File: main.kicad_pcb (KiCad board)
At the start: 2 copper layers, 32 x 32 mm, 46 parts, among them J1 USB_OTG, J2 Conn_01x02, J4 Conn_01x02, J5 Conn_02x03_Odd_Even, J6 Conn_01x02, Q1 Q_PMOS_GSD, Q2 NTLJF3117P, SW1 SW_Push, SW2 SW_SPDT, U1 LTC2955-1(DFN), U2 LTC3458, U3 ATTINY13-20SSU, U4 MCP73831

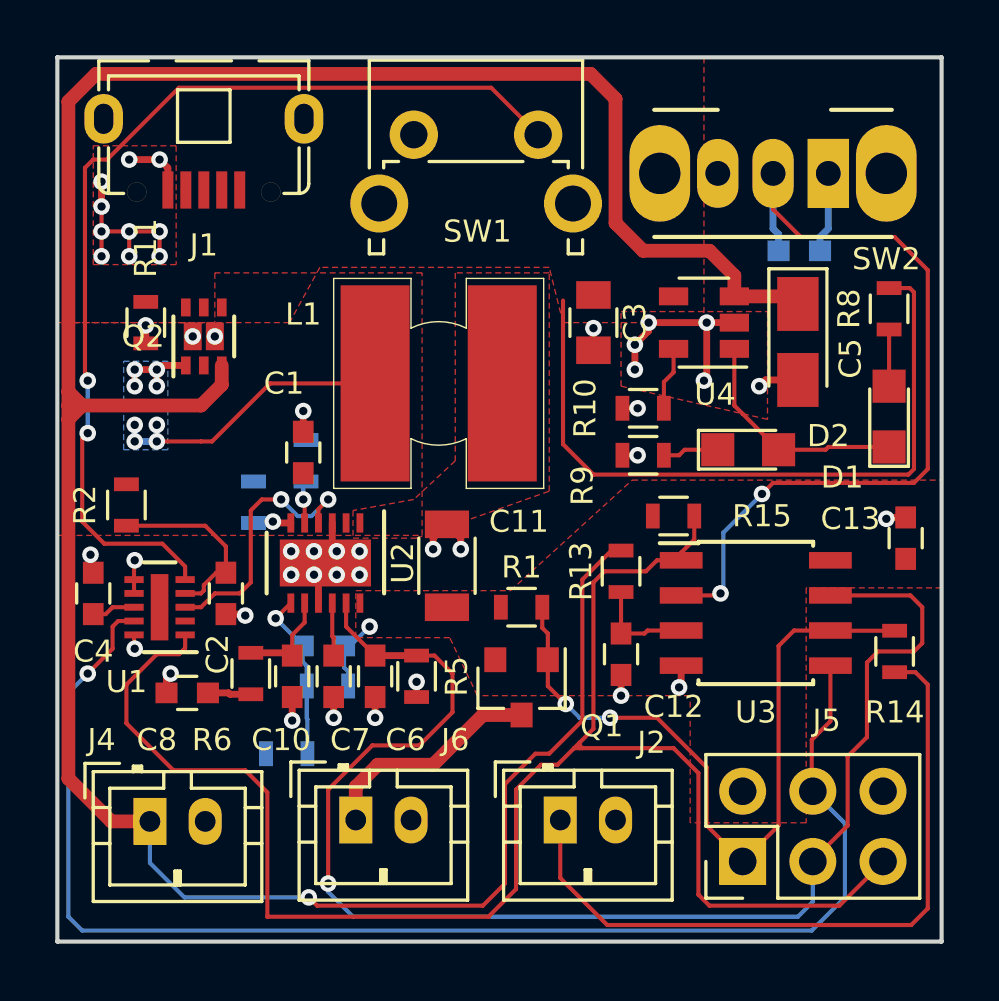
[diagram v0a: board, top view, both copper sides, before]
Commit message: Fixed NTLJF3117P MOSFET pin layout
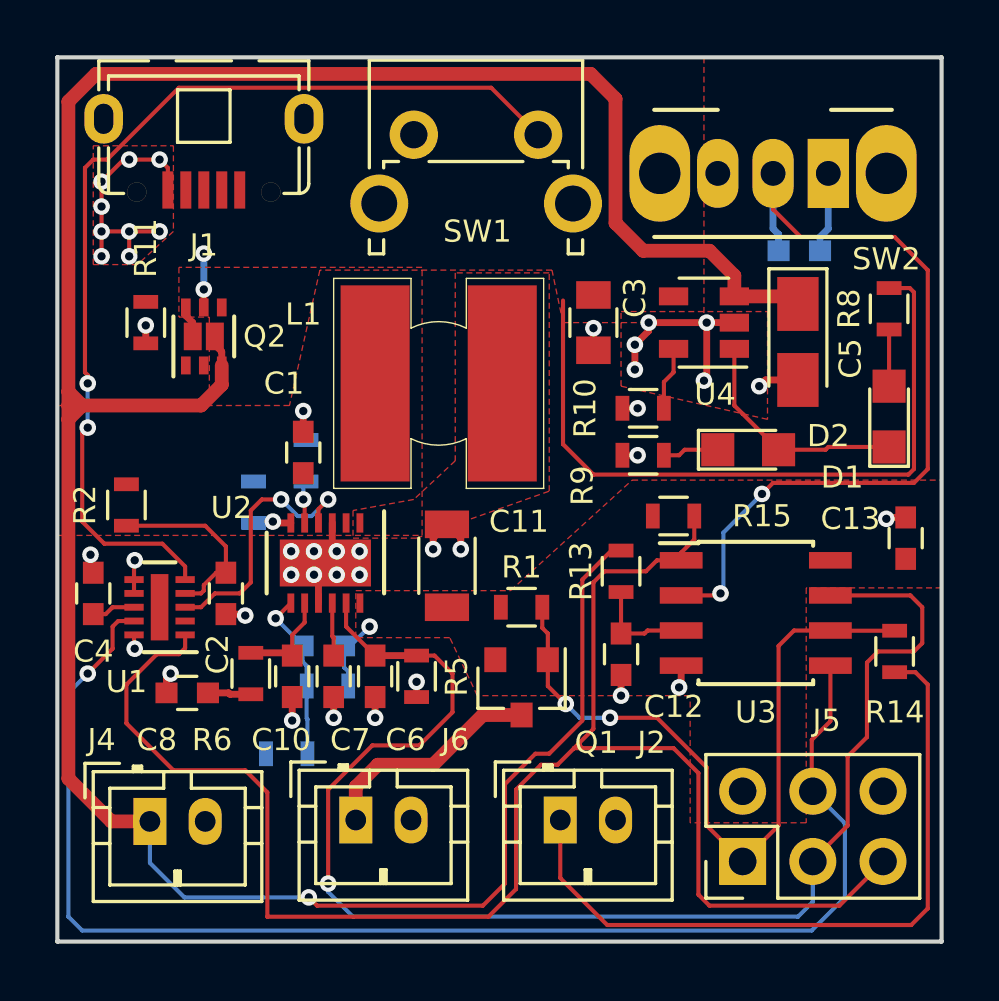
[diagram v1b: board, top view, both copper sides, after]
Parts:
- D1: value LED -> Red LED
- D2: value LED -> Green LED
- Q1: value Q_PMOS_GSD -> DMP1045U
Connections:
- Q2 pad 1: /Power Supply/DC/DC boost converter/Vsup -> /Power Supply/VUSB
- Q2 pad 6: /Power Supply/VUSB -> /Power Supply/DC/DC boost converter/Vsup
- Q2 pad 7: GND -> /Power Supply/DC/DC boost converter/Vsup
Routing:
- net /Power Supply/DC/DC boost converter/Vsup: track 13.9 -> 1.15 mm, vias 8 -> 0
- net GND: track 30.6 -> 37.7 mm, vias 37 -> 42
- net (no net): track 6.60 -> 0.00 mm, vias 8 -> 0
- net /Power Supply/VUSB: track 25.8 -> 27.8 mm, vias 0 -> 2
- net /BAT+: track 99.0 -> 100.2 mm
- removed copper zone on B.Cu, net /Power Supply/DC/DC boost converter/Vsup
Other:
- board text added: "Programmable Heater v1.1 Design: Patrick Baus Date: 2017-10 https://github.com/PatrickBaus"
- board text removed: "Programmable Heater Design: Patrick Baus Date: 2017-10 https://github.com/PatrickBaus"

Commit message: Moved MCU pins around to make sure that they do not interfere with the programmer Moved ISP Header closer to the edge of the board to allow easier access with the programmer Added pulldown resistor to the DCD/DC converters enable pin to make sure it stays off in case of failure Added more PDFs of components
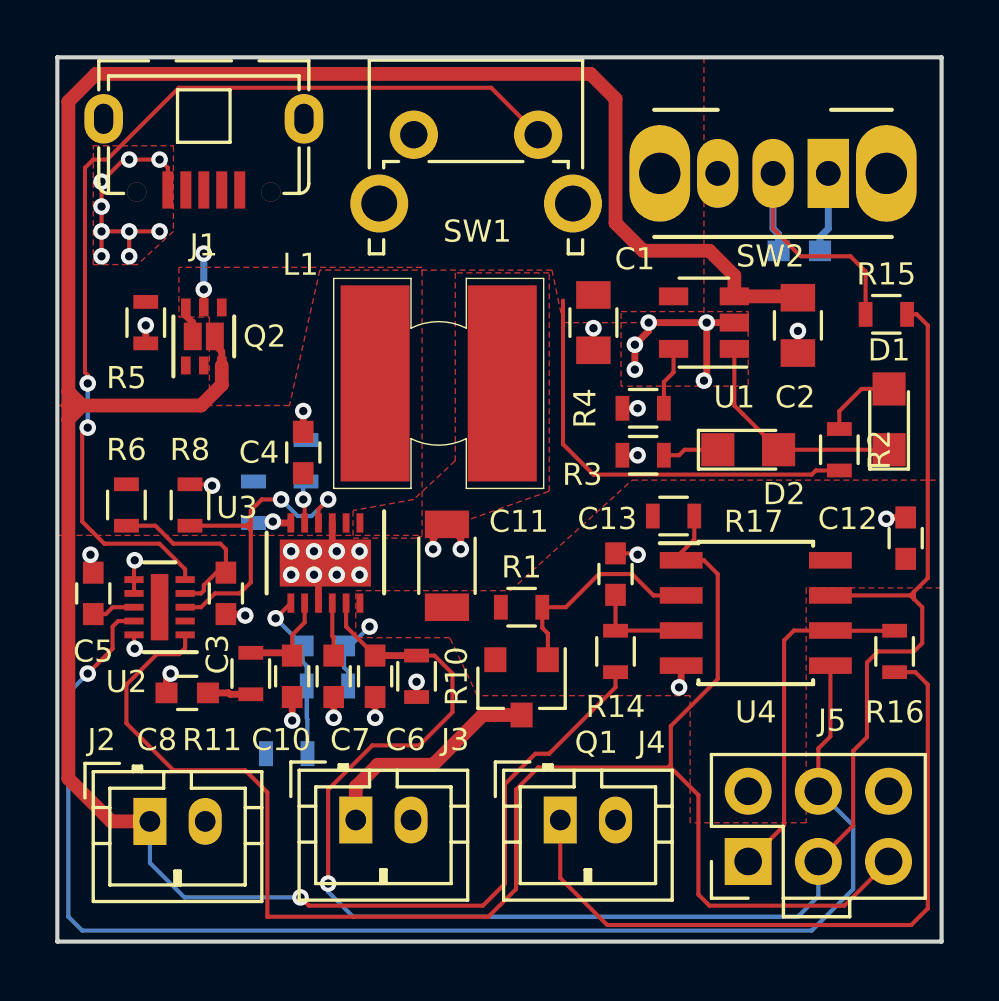
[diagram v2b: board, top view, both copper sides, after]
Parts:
- removed the C5 at (116.8, 80.3)
- added C2: 10u, Capacitors_SMD:C_0805, F.Cu at (116.8, 79.7)
- added R15: 4.7k, Resistors_SMD:R_0603, F.Cu at (120.0, 79.3)
- added R8: 100k, Resistors_SMD:R_0603, F.Cu at (94.8, 86.2)
- J5: value Conn_02x03_Odd_Even -> AVR-ISP-6
- moved R2 5.41 mm to (118.3, 84.2), turned to 270 degrees
- moved R14 2.91 mm to (110.2, 91.5), turned to 270 degrees
- moved C13 2.91 mm to (110.2, 88.7), turned to 90 degrees
- moved J5 0.20 mm to (115.0, 99.1)
- moved D1 0.10 mm to (120.1, 83.1)
- renumbered C3 to C1, C13 to C12, C12 to C13, C2 to C3, C1 to C4, C4 to C5, J4 to J2, J6 to J3, J2 to J4, R5 to R10, R6 to R11, R7 to R12, R12 to R13, R13 to R14, R14 to R16, R15 to R17, R8 to R2, R9 to R3, R10 to R4, R11 to R5, R2 to R6, R3 to R7, R4 to R9, U4 to U1, U1 to U2, U2 to U3, U3 to U4
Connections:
- C6 pad 1: /Microcontroller/~enable_burst -> Net-(C6-Pad1)
- J5 pad 1: /Microcontroller/~enable_heater -> /Microcontroller/MISO
- J5 pad 3: /Microcontroller/~enable_burst -> /Microcontroller/SCK
- J5 pad 5: /Power Supply/Power_down_warning -> /Microcontroller/RST
- R10 pad 1: /Microcontroller/~enable_burst -> Net-(C6-Pad1)
- R16 pad 1: /Microcontroller/~enable_heater -> /Microcontroller/MISO
- R17 pad 2: /Power Supply/Power_down_warning -> /Microcontroller/RST
- U2 pad 1: /Power Supply/Power_down_warning -> Net-(U2-Pad1)
- U3 pad 11: /Microcontroller/~enable_burst -> Net-(C6-Pad1)
- U4 pad 1: /Power Supply/Power_down_warning -> /Microcontroller/RST
- U4 pad 2: Net-(C14-Pad1) -> /Microcontroller/~enable_heater
- U4 pad 6: /Microcontroller/~enable_heater -> /Microcontroller/MISO
- U4 pad 7: /Microcontroller/~enable_burst -> /Microcontroller/SCK
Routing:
- net /Power Supply/Power_down_warning: track 59.6 -> 0.00 mm
- net /Microcontroller/RST: track 0.00 -> 56.5 mm
- net /Microcontroller/~enable_burst: track 50.9 -> 0.00 mm, vias 1 -> 0
- net /Microcontroller/SCK: track 0.00 -> 44.7 mm
- net Net-(C14-Pad1): track 29.9 -> 10.4 mm, vias 2 -> 0
- net /Microcontroller/~enable_heater: track 26.6 -> 7.83 mm, vias 2 -> 0
- net Net-(C6-Pad1): track 0.00 -> 17.4 mm, vias 0 -> 1
- net /Microcontroller/MISO: track 0.00 -> 12.7 mm
- net /Power Supply/VUSB: track 27.8 -> 17.7 mm
- net /BAT+: track 100.2 -> 95.5 mm
- net Net-(R8-Pad1): track 9.81 -> 12.5 mm
- net Net-(U2-Pad1): track 0.00 -> 1.59 mm
- net Net-(D1-Pad2): track 2.05 -> 2.78 mm
- net GND: track 37.7 -> 37.9 mm, vias 42 -> 43
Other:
- board text added: "Programmable Heater v1.1 Design: Patrick Baus Date: 2018-01 https://github.com/PatrickBaus"
- board text removed: "Programmable Heater v1.1 Design: Patrick Baus Date: 2017-10 https://github.com/PatrickBaus"

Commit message: Preparing for v1.2 Updated to KiCAD 5 nightly Added resistors to isolate the programming pins Added transistor to drive the LED Replaced LTC3458 boost converter with an LTC3536 buck-boost converter to step down the USB power supply Added debugging jumper to test the voltage regulator
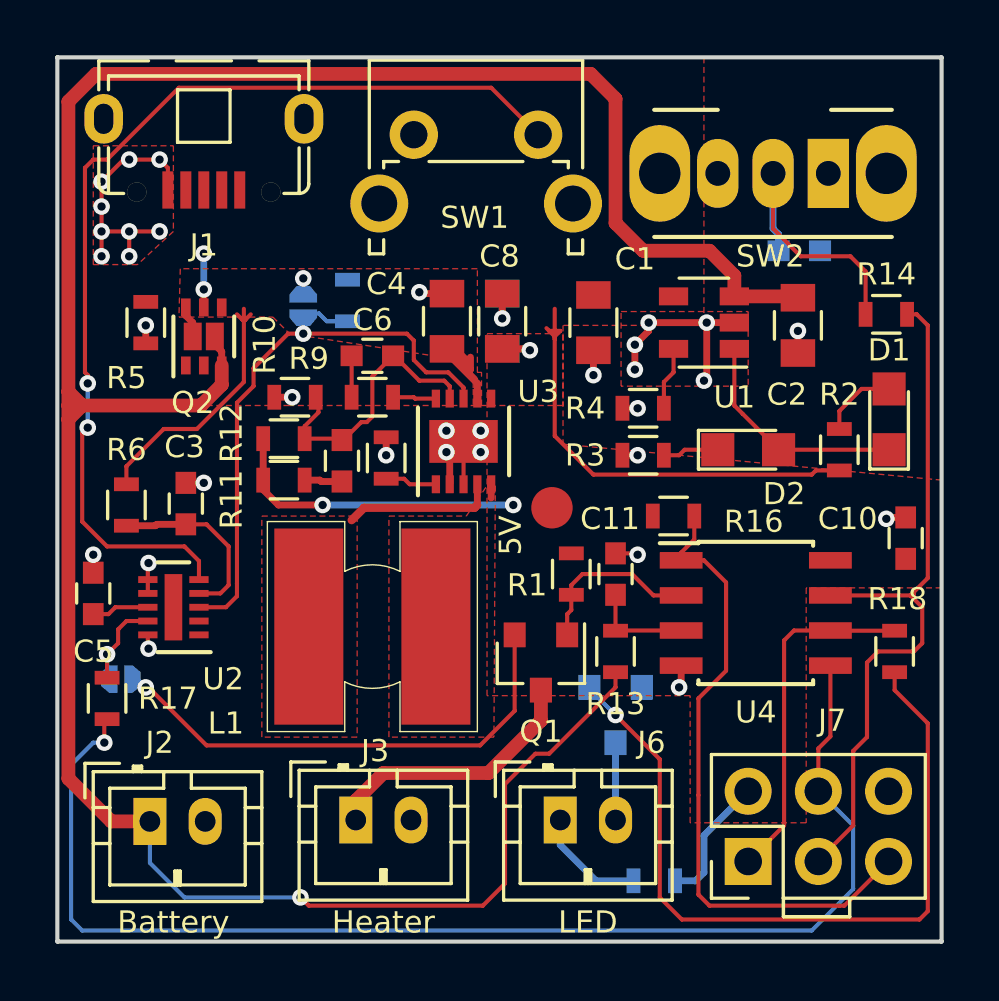
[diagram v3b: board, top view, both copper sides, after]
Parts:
- removed the C10 at (98.5, 92.4)
- removed the C11 at (104.1, 88.4)
- removed the R13 at (98.3, 95.2)
- removed REF***: OSHW-Logo_7.5x8mm_SilkScreen, Symbols:OSHW-Logo_7.5x8mm_SilkScreen
- added J4: GS2, Custom_footprints:jumper_solder_small, B.Cu at (98.9, 79.0)
- added J5: GS2, Custom_footprints:jumper_solder_small, B.Cu at (92.3, 92.5)
- added J8: Conn_01x01, Measurement_Points:Measurement_Point_Round-SMD-Pad_Small, F.Cu at (107.9, 86.3)
- added Q3: MMBT3904, TO_SOT_Packages_SMD:SOT-23, B.Cu at (110.2, 93.8)
- added R17: 4.7k, Resistors_SMD:R_0603, F.Cu at (91.8, 93.2)
- added R18: 4.7k, Resistors_SMD:R_0603, F.Cu at (120.3, 91.5)
- C4: value 2.2u -> 47u; footprint Capacitors_SMD:C_0603 -> Capacitors_SMD:C_0805
- C6: value 10n -> 200p
- C7: value 10n -> 18p
- C8: value 560p -> 47u; footprint Capacitors_SMD:C_0603 -> Capacitors_SMD:C_0805
- C9: value 10p -> 47u; footprint Capacitors_SMD:C_0603 -> Capacitors_SMD:C_0805
- R10: value 133k -> 150k
- R11: value 33k -> 22.6k
- R12: value 1M -> 1.1M; moved to F.Cu
- R15: renamed from R16; moved to B.Cu
- R7: renamed from R8; moved to B.Cu
- R8: renamed from R7; value 450k -> 332k; moved to F.Cu
- R9: value 124k -> 33k; moved to F.Cu
- SW1: footprint SW_Tactile_SPST_Angled_PTS645Vx31-2LFS -> Buttons_Switches_THT:SW_Tactile_SPST_Angled_PTS645Vx31-2LFS
- U3: value LTC3458 -> LTC3536; footprint Housings_DFN_QFN:DFN-12-1EP_3x4mm_Pitch0.5mm -> Housings_DFN_QFN:DFN-10-1EP_3x3mm_Pitch0.5mm
- U4: value ATTINY13-20SSU -> ATTINY13
- moved C8 17.6 mm to (106.1, 79.5), turned to 90 degrees
- moved C9 13.4 mm to (106.1, 79.5), turned to 90 degrees
- moved R15 12.0 mm to (111.6, 99.8), turned to 180 degrees
- moved C6 11.6 mm to (101.4, 80.8), turned to 0 degrees
- moved R10 11.0 mm to (98.6, 82.3), turned to 180 degrees
- moved R7 9.34 mm to (100.5, 78.8)
- moved L1 9.12 mm to (101.4, 90.6)
- moved R12 9.09 mm to (98.2, 83.8), turned to 0 degrees
- moved C7 7.81 mm to (100.3, 84.6), turned to 90 degrees
- moved R11 7.10 mm to (98.2, 85.3), turned to 0 degrees
- moved C4 7.04 mm to (104.1, 79.5)
- moved U3 6.66 mm to (104.7, 83.9), turned to 90 degrees
- moved R8 5.06 mm to (101.9, 84.5)
- moved C3 3.56 mm to (94.7, 86.2), turned to 90 degrees
- moved R9 3.32 mm to (101.4, 82.3), turned to 0 degrees
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- renumbered C12 to C10, C13 to C11, C14 to C12, J4 to J6, J5 to J7, R14 to R13, R15 to R14, R17 to R16
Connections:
- C6 pad 2: GND -> Net-(C6-Pad2)
- C7 pad 2: GND -> Net-(C6-Pad2)
- C8 pad 1: Net-(C8-Pad1) -> /Power Supply/V+5
- C9 pad 2: Net-(C9-Pad2) -> GND
- J6 pad 2: GND -> Net-(J6-Pad2)
- J7 pad 4: /Power Supply/Kill_power -> /Microcontroller/MOSI
- L1 pad 1: /Power Supply/DC/DC boost converter/Vsup -> Net-(L1-Pad1)
- R10 pad 1: Net-(C6-Pad1) -> Net-(C6-Pad2)
- R11 pad 1: Net-(C10-Pad1) -> /Power Supply/V+5
- R11 pad 2: Net-(C8-Pad1) -> Net-(C7-Pad1)
- R12 pad 2: Net-(C9-Pad2) -> Net-(C6-Pad2)
- R15 pad 1: /Microcontroller/MISO -> /Power Supply/V+5
- R7 pad 1: Net-(R8-Pad1) -> Net-(J4-Pad2)
- R8 pad 1: Net-(R7-Pad1) -> Net-(R8-Pad1)
- R9 pad 1: Net-(R9-Pad1) -> Net-(C6-Pad1)
- R9 pad 2: GND -> Net-(R9-Pad2)
- U2 pad 3: Net-(R8-Pad1) -> Net-(J4-Pad2)
- U2 pad 9: /Power Supply/Kill_power -> /Power Supply/~Kill_power
- U3 pad 1: Net-(L1-Pad2) -> Net-(R8-Pad1)
- U3 pad 10: Net-(C7-Pad1) -> Net-(R9-Pad2)
- U3 pad 11: Net-(C6-Pad1) -> GND
- U3 pad 2: /Power Supply/DC/DC boost converter/Vsup -> GND
- U3 pad 4: Net-(R8-Pad1) -> Net-(L1-Pad1)
- U3 pad 5: Net-(R9-Pad1) -> Net-(L1-Pad2)
- U3 pad 6: Net-(R7-Pad1) -> /Power Supply/V+5
- U3 pad 7: Net-(C9-Pad2) -> /Power Supply/DC/DC boost converter/Vsup
- U3 pad 8: Net-(C10-Pad1) -> Net-(J4-Pad2)
- U3 pad 9: GND -> Net-(C6-Pad2)
- U4 pad 5: /Power Supply/Kill_power -> /Microcontroller/MOSI
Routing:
- net /Power Supply/Kill_power: track 50.1 -> 0.00 mm, vias 1 -> 0
- net /Microcontroller/MOSI: track 0.00 -> 45.9 mm, vias 0 -> 1
- net /Power Supply/V+5: track 2.73 -> 36.1 mm, vias 1 -> 4
- net /Microcontroller/RST: track 56.5 -> 23.2 mm
- net Net-(Q3-Pad1): track 0.00 -> 28.0 mm, vias 0 -> 1
- net Net-(J4-Pad2): track 0.00 -> 22.2 mm, vias 0 -> 1
- net Net-(J6-Pad1): track 25.8 -> 4.09 mm
- net /Microcontroller/SCK: track 44.7 -> 26.2 mm
- net /Power Supply/DC/DC boost converter/Vsup: track 1.15 -> 17.6 mm, vias 0 -> 1
- net Net-(C6-Pad1): track 17.4 -> 1.50 mm, vias 1 -> 0
- net Net-(R8-Pad1): track 12.5 -> 1.88 mm, vias 2 -> 0
- net Net-(C6-Pad2): track 0.00 -> 10.00 mm
- net Net-(C9-Pad2): track 6.15 -> 0.00 mm, vias 1 -> 0
- net Net-(L1-Pad1): track 0.00 -> 5.53 mm
- net GND: track 37.9 -> 32.7 mm, vias 43 -> 34
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- added copper zone on F.Cu, net Net-(L1-Pad1)
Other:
- board text added: "5V"
- board text added: "A"
- board text added: "C"
- board text added: "GND"
- board text added: "MISO"
- board text added: "MOSI"
- board text added: "Programmable Heater v1.2 Design: Patrick Baus Date: 2018-03 https://github.com/PatrickBaus"
- board text added: "RST"
- board text added: "SCK"
- board text added: "U3 no shutdown"
- board text added: "always enable U3"
- board text removed: "Programmable Heater v1.1 Design: Patrick Baus Date: 2018-01 https://github.com/PatrickBaus"

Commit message: Updated to Kicad v5.0
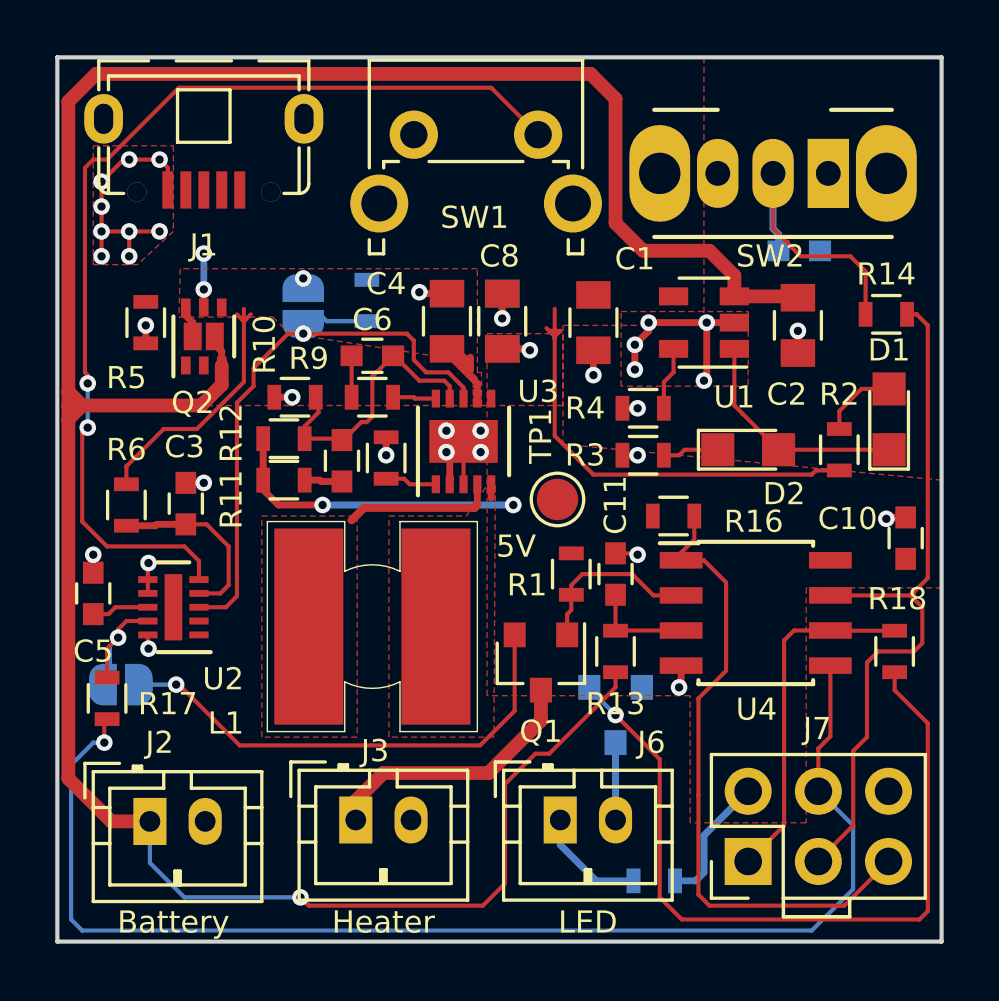
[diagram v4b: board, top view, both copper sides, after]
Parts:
- removed J4, J5: GS2, Custom_footprints:jumper_solder_small
- removed J8: Conn_01x01, Measurement_Points:Measurement_Point_Round-SMD-Pad_Small
- added JP1: SolderJumper_2_Open, Jumper:SolderJumper-2_P1.3mm_Open_RoundedPad1.0x1.5mm, B.Cu at (98.9, 79.0)
- added JP2: SolderJumper_2_Open, Jumper:SolderJumper-2_P1.3mm_Open_RoundedPad1.0x1.5mm, B.Cu at (92.3, 92.7)
- added LOGO1: Logo_Open_Hardware_Small, Symbol:OSHW-Logo_7.5x8mm_SilkScreen, B.Cu at (94.5, 86.3)
- added TP1: Test_Point, TestPoint:TestPoint_Pad_D1.5mm, F.Cu at (108.1, 86.0)
- J1: value USB_OTG -> USB_MICRO
- J7: footprint Pin_Headers:Pin_Header_Straight_2x03_Pitch2.54mm -> Connector_PinHeader_2.54mm:PinHeader_2x03_P2.54mm_Vertical
- R3: value 470 -> 1k
- U4: value ATTINY13 -> ATtiny13-20SSU; footprint Housings_SOIC:SOIC-8_3.9x4.9mm_Pitch1.27mm -> Package_SO:SOIC-8_3.9x4.9mm_P1.27mm
- moved R7 0.70 mm to (101.2, 78.8)
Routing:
- net /Power Supply/~Kill_power: track 4.25 -> 5.14 mm
- net Net-(JP1-Pad2): track 22.2 -> 22.9 mm
